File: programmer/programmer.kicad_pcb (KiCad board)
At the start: 2 copper layers, 34.3 x 27.3 mm, 16 parts, among them J1 10118192-0001LF, J2 Conn_02x05_Odd_Even, Q1 Q_NMOS_GSD, SW1 222CMVBAR, SW2 222CMVBAR, U1 FT230XS-R

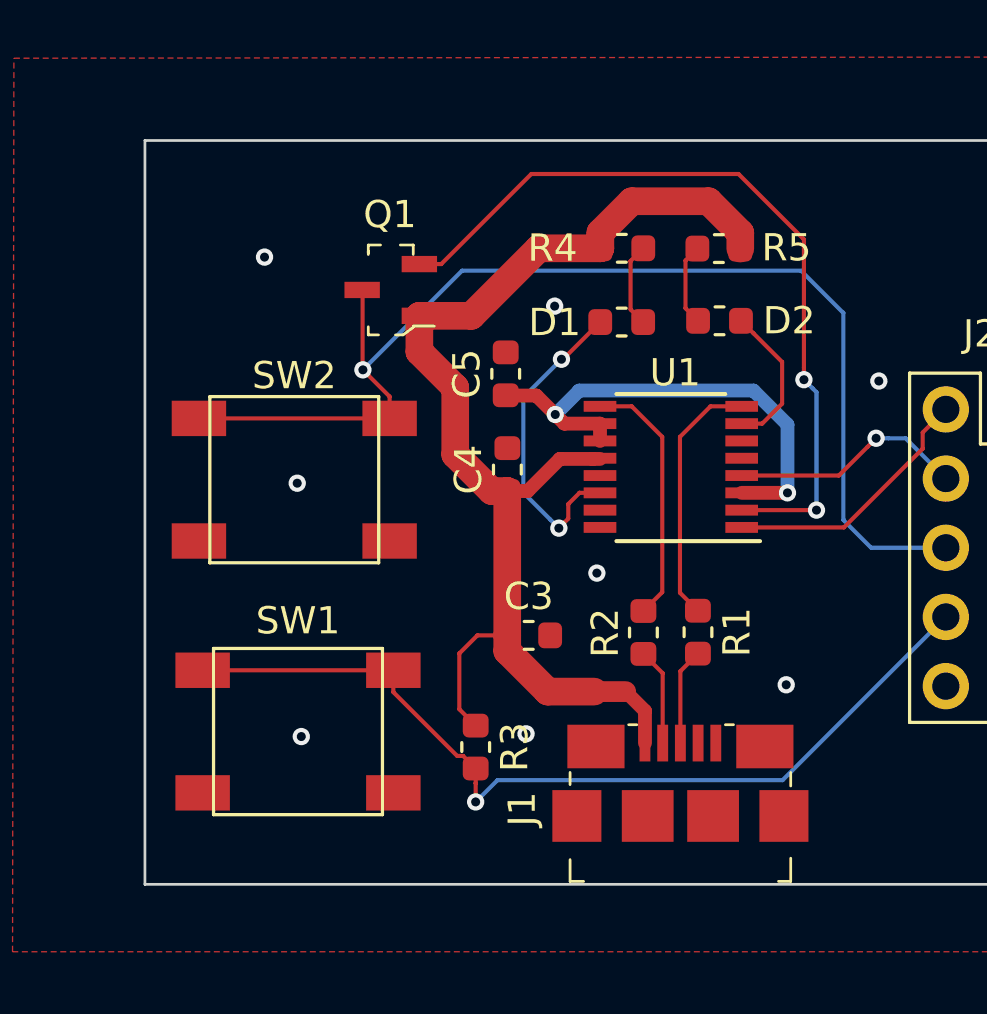
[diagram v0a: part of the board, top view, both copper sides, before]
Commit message: Changed programmer parts to LCSC parts, added part numbers
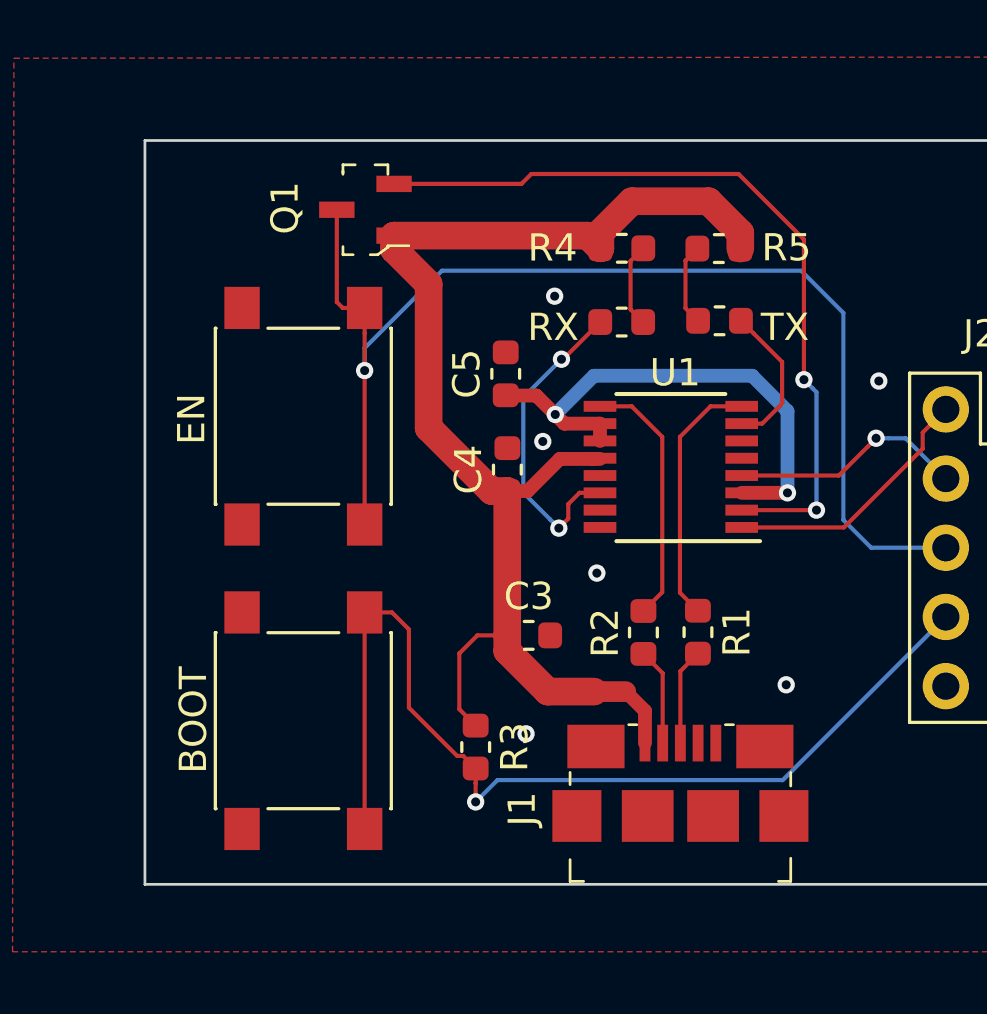
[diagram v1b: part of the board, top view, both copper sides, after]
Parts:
- SW1, SW2: value 222CMVBAR -> SW_SPST; footprint My Footprints:222CMVBAR -> Button_Switch_SMD:SW_Push_1P1T_NO_6x6mm_H9.5mm
- moved Q1 3.09 mm to (126.2, 105.4)
- moved SW2 2.35 mm to (123.9, 113.0), turned to 90 degrees
- moved SW1 0.44 mm to (123.9, 124.2), turned to 90 degrees
- renumbered D1 to RX1, D2 to TX1
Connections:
- SW1 pad 2: GND -> BOOT
- SW2 pad 2: GND -> EN
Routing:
- net BOOT: track 33.3 -> 37.4 mm
- net VBUS: track 44.9 -> 48.3 mm
- net +3V3: track 18.1 -> 18.9 mm
- net GND: vias 8 -> 6
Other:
- board text added: "BOOT"
- board text added: "EN"
- board text added: "RX"
- board text added: "TX"

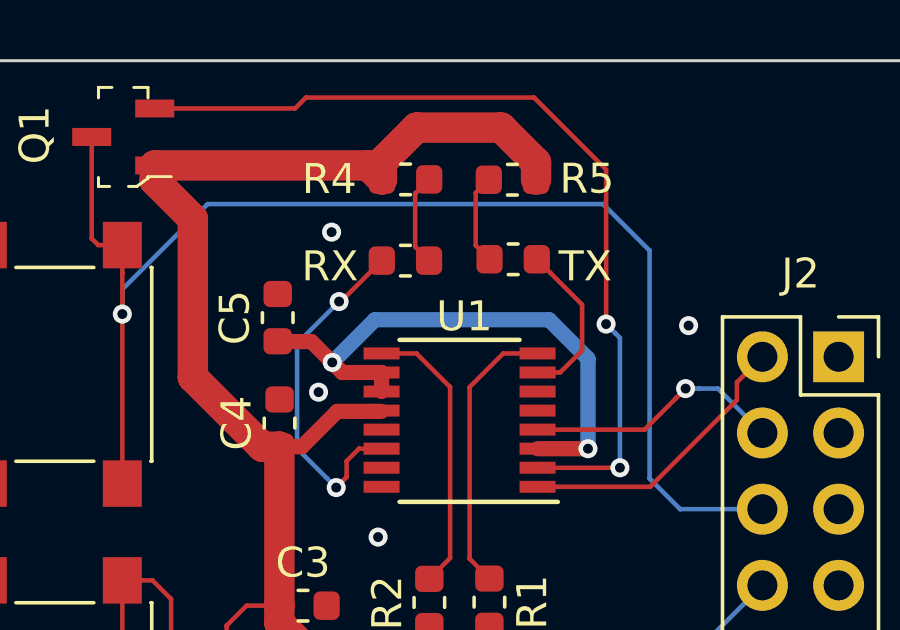
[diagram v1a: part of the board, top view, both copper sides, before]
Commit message: Moved connector and added silkscreen labels on product board
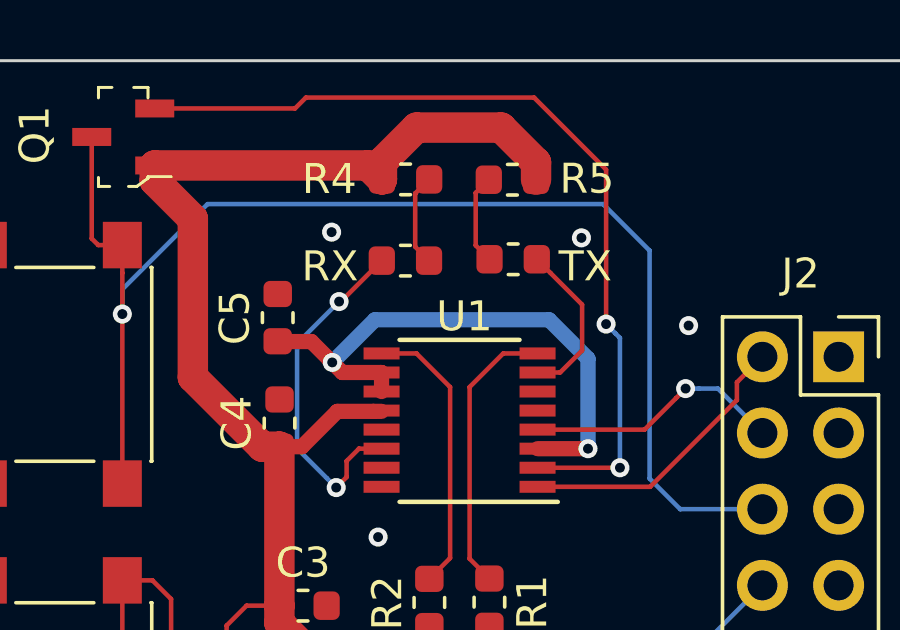
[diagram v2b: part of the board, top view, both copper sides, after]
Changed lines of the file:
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@@
       (drillshape 0)
       (scaleselection 1)
-      (outputdirectory "Gerber/"))
+      (outputdirectory "Gerbers/Gerber Files/"))
   )
   (net 0 "")
@@
   (via (at 145.05 111.7) (size 0.635) (drill 0.3302) (layers F.Cu B.Cu) (net 1))
   (via (at 133.15 108.585) (size 0.635) (drill 0.3302) (layers F.Cu B.Cu) (net 1))
-  (via (at 132.715 113.919) (size 0.635) (drill 0.3302) (layers F.Cu B.Cu) (net 1))
+  (via (at 141.478 108.7755) (size 0.635) (drill 0.3302) (layers F.Cu B.Cu) (net 1))
   (segment (start 131.40944 115.74292) (end 131.41452 115.73784) (width 1.016) (layer F.Cu) (net 2))
   (segment (start 131.40944 121.03608) (end 131.40944 115.74292) (width 1.016) (layer F.Cu) (net 2))

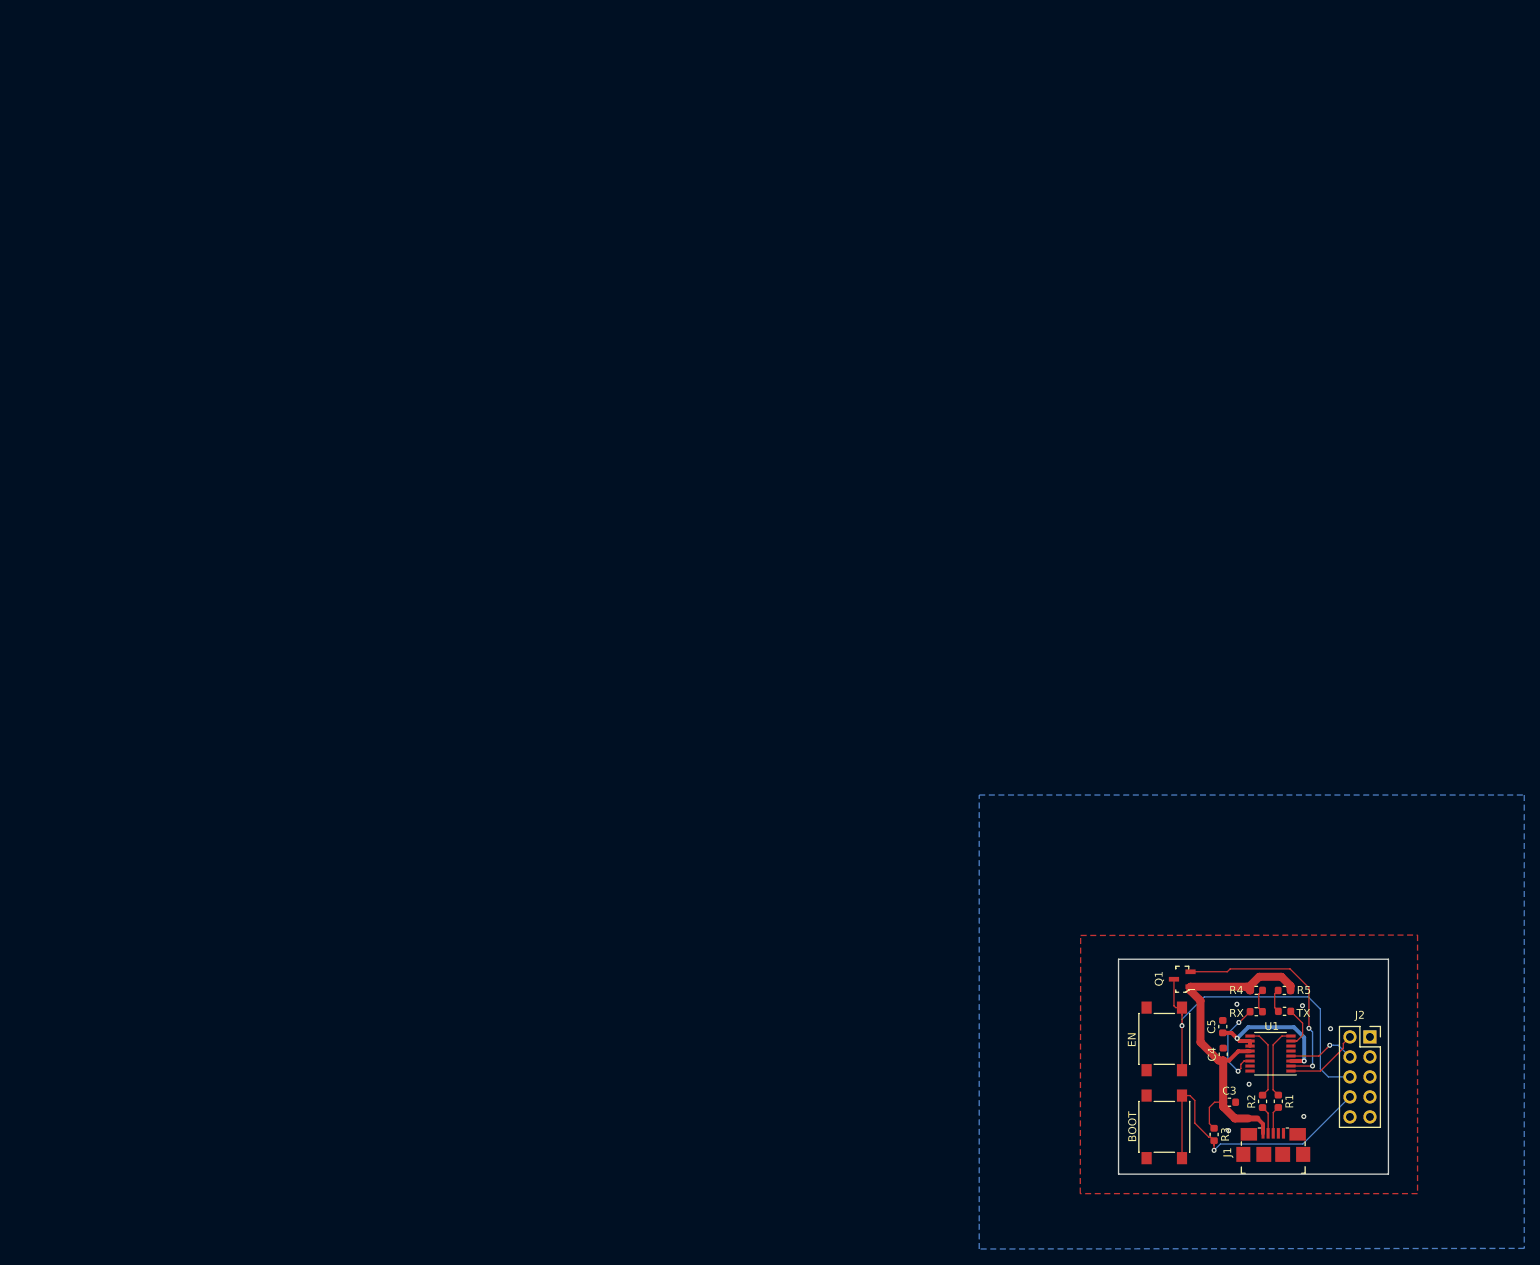
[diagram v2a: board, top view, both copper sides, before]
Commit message: Updated programmer to include jtag and dtr signals. Swapped FT230X for FT2232HL
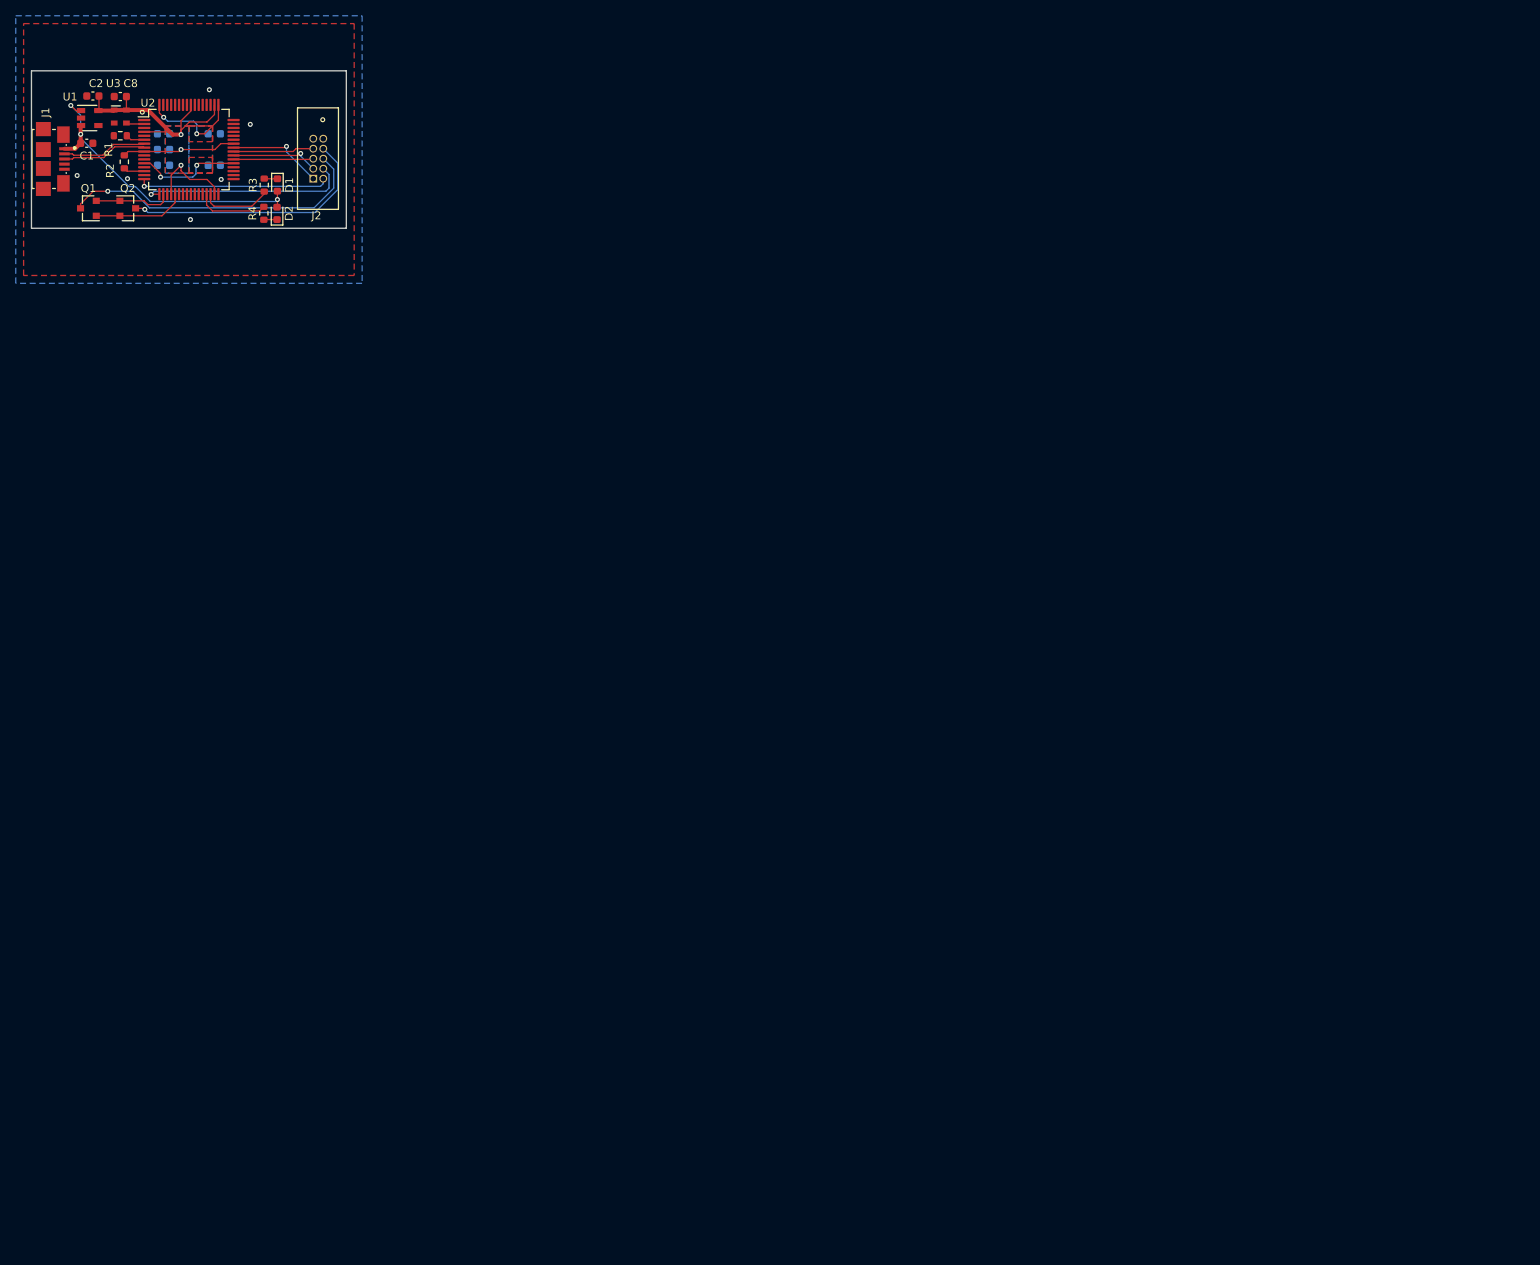
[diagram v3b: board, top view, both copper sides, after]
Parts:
- removed C4: 0.1uF, Capacitor_SMD:C_0603_1608Metric
- removed R5: 270, Capacitor_SMD:C_0603_1608Metric
- removed RX1, TX1: LED, Capacitor_SMD:C_0603_1608Metric
- removed SW1, SW2: SW_SPST, Button_Switch_SMD:SW_Push_1P1T_NO_6x6mm_H9.5mm
- added C1: 0.1uF, Capacitor_SMD:C_0603_1608Metric, F.Cu at (-13.0, -0.80)
- added C2: 0.1uF, Capacitor_SMD:C_0603_1608Metric, F.Cu at (-12.2, -6.80)
- added C6: 0.1uF, Capacitor_SMD:C_0603_1608Metric, B.Cu at (-3.23, 0.00)
- added C7: 0.1uF, Capacitor_SMD:C_0603_1608Metric, B.Cu at (-3.23, 2.00)
- added C8: 0.1uF, Capacitor_SMD:C_0603_1608Metric, F.Cu at (-8.71, -6.73)
- added C9: 0.1uF, Capacitor_SMD:C_0603_1608Metric, B.Cu at (-3.23, -2.00)
- added D1: BLU, LED_SMD:LED_0603_1608Metric, F.Cu at (11.2, 4.50)
- added D2: GRN, LED_SMD:LED_0603_1608Metric, F.Cu at (11.2, 8.11)
- added Q2: Q_NMOS_GSD, Package_TO_SOT_SMD:SOT-23, F.Cu at (-7.77, 7.47)
- added U2: FT2232HL, Package_QFP:LQFP-64_10x10mm_P0.5mm, F.Cu at (0.00, 0.00)
- added U3: ASDMB-12.000MHz, Oscillator:Oscillator_SMD_Abracon_ASDMB-4Pin_2.5x2.0mm, F.Cu at (-8.71, -4.19)
- C3: value 4.7uF -> 3.3uF; moved to B.Cu
- C5: moved to B.Cu
- J1: footprint digikey-footprints:USB_Micro_B_Female_10118192 -> Esper_Footprints:AMPHENOL_10118192-0001LF
- J2: footprint Connector_PinSocket_2.54mm:PinSocket_2x05_P2.54mm_Vertical -> Esper_Footprints:CNC_3220-10-0100-00
- Q1: footprint digikey-footprints:SOT-23-3 -> Package_TO_SOT_SMD:SOT-23
- R1, R2: value 27 -> 12K; footprint Capacitor_SMD:C_0603_1608Metric -> Resistor_SMD:R_0603_1608Metric
- R3: value 10K -> 470; footprint Capacitor_SMD:C_0603_1608Metric -> Resistor_SMD:R_0603_1608Metric
- R4: value 270 -> 470; footprint Capacitor_SMD:C_0603_1608Metric -> Resistor_SMD:R_0603_1608Metric
- U1: value FT230XS-R -> TLV75533PDBV; footprint Package_SO:SSOP-16_3.9x4.9mm_P0.635mm -> Package_TO_SOT_SMD:SOT-23-5
- moved J1 198.9 mm to (-15.8, 1.20), turned to 270 degrees
- moved R1 191.6 mm to (-8.71, -1.75), turned to 180 degrees
- moved U1 191.4 mm to (-12.6, -4.00), turned to 0 degrees
- moved R2 187.5 mm to (-8.21, 1.56), turned to 90 degrees
- moved C3 178.2 mm to (3.23, -2.00)
- moved J2 173.0 mm to (15.8, 3.70), turned to 180 degrees
- moved R3 170.6 mm to (9.57, 4.51)
- moved Q1 170.0 mm to (-12.8, 7.47)
- moved C5 168.5 mm to (3.23, 2.00), turned to 0 degrees
- moved R4 160.1 mm to (9.52, 8.10), turned to 90 degrees
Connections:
- C3 pad 1: VBUS -> +1V8
- C5 pad 1: +3V3 -> +1V8
- J1 pad 2: Net-(J1-Pad2) -> D-
- J1 pad 3: Net-(J1-Pad3) -> D+
- J2 pad 1: Net-(J2-Pad1) -> TMS
- J2 pad 3: Net-(J2-Pad3) -> TDI
- J2 pad 5: Net-(J2-Pad5) -> TCK
- J2 pad 7: Net-(J2-Pad7) -> TDO
- J2 pad 8: BOOT -> IO0
- Q1 pad 1: VBUS -> DTR#
- Q1 pad 2: nRTS -> RTS#
- R1 pad 1: D+ -> /REF
- R1 pad 2: Net-(J1-Pad3) -> GND
- R2 pad 1: D- -> /RESET
- R2 pad 2: Net-(J1-Pad2) -> +3V3
- R3 pad 1: VBUS -> Net-(D1-Pad1)
- R3 pad 2: BOOT -> TXLED#
- R4 pad 1: VBUS -> Net-(D2-Pad1)
- R4 pad 2: Net-(R4-Pad2) -> RXLED#
- U1 pad 1: TX -> VBUS
- U1 pad 2: nRTS -> GND
- U1 pad 3: +3V3 -> VBUS
- U1 pad 4: RX -> Net-(U1-Pad4)
- U1 pad 5: GND -> +3V3
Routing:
- net BOOT: track 37.4 -> 0.00 mm, vias 1 -> 0
- net +3V3: track 18.9 -> 55.5 mm, vias 2 -> 3
- net IO0: track 0.00 -> 33.1 mm, vias 0 -> 1
- net nRTS: track 29.1 -> 0.00 mm, vias 2 -> 0
- net +1V8: track 0.00 -> 26.6 mm, vias 0 -> 4
- net RX: track 8.68 -> 26.8 mm
- net TX: track 9.64 -> 24.4 mm, vias 0 -> 1
- net TMS: track 0.00 -> 12.3 mm, vias 0 -> 1
- net DTR#: track 0.00 -> 11.8 mm
- net Net-(RX1-Pad1): track 11.7 -> 0.00 mm, vias 2 -> 0
- net TDI: track 0.00 -> 11.2 mm, vias 0 -> 1
- net TDO: track 0.00 -> 10.3 mm
- net TCK: track 0.00 -> 10.2 mm
- net RTS#: track 0.00 -> 9.84 mm
- net RXLED#: track 0.00 -> 9.18 mm
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- added copper zone on B.Cu, net +1V8
- added copper zone on F.Cu, net +1V8
- added copper zone on B.Cu, net +3V3
- added copper zone on F.Cu, net +3V3
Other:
- board size 34.3 x 27.3 mm -> 40 x 20 mm
- board text removed: "BOOT"
- board text removed: "EN"
- board text removed: "RX"
- board text removed: "TX"
